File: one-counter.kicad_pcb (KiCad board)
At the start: 2 copper layers, 19.1 x 50.8 mm, 15 parts, among them J1 Conn_01x07-L, J2 Conn_01x07-R, U1 L7805, U2 555-L, U3 555-R, U4 74LS90-L, U5 74LS90-R, U6 7447-L, U7 7447-R, U8 5082-7650-L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

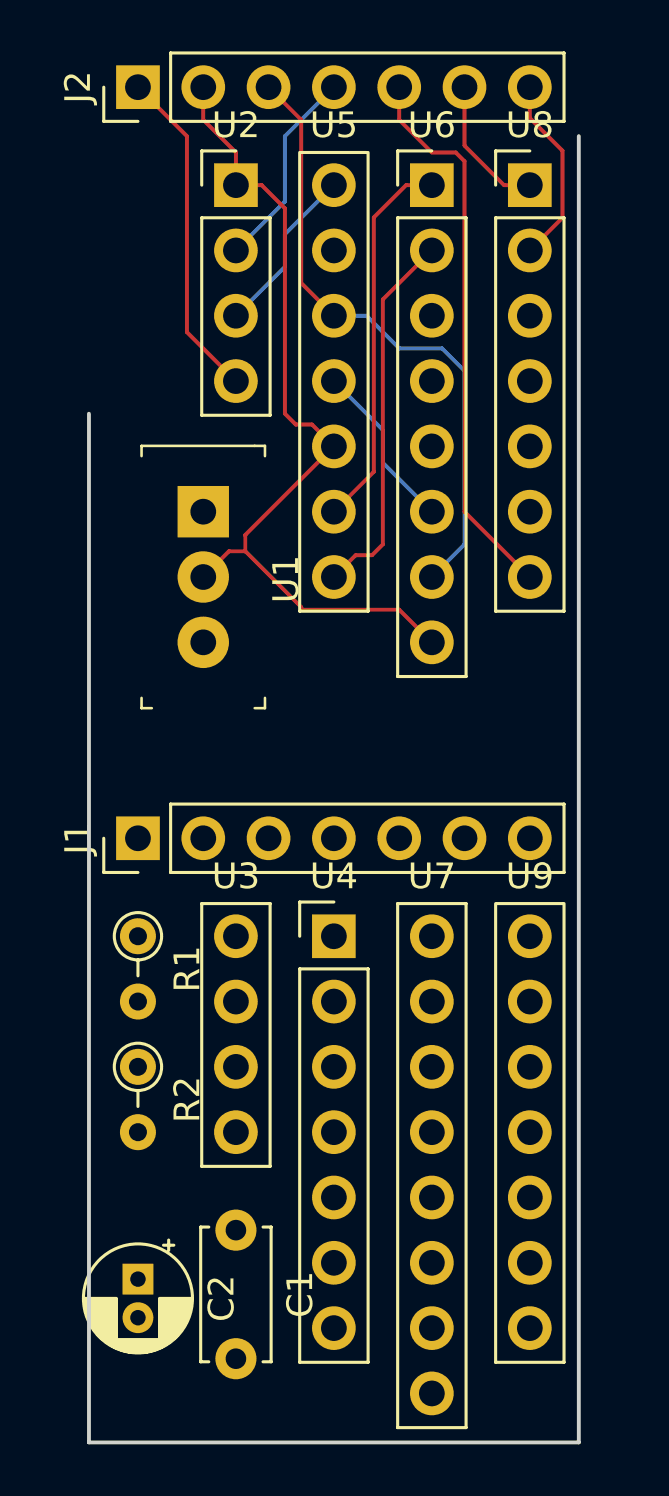
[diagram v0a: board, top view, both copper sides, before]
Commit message: route bottom half
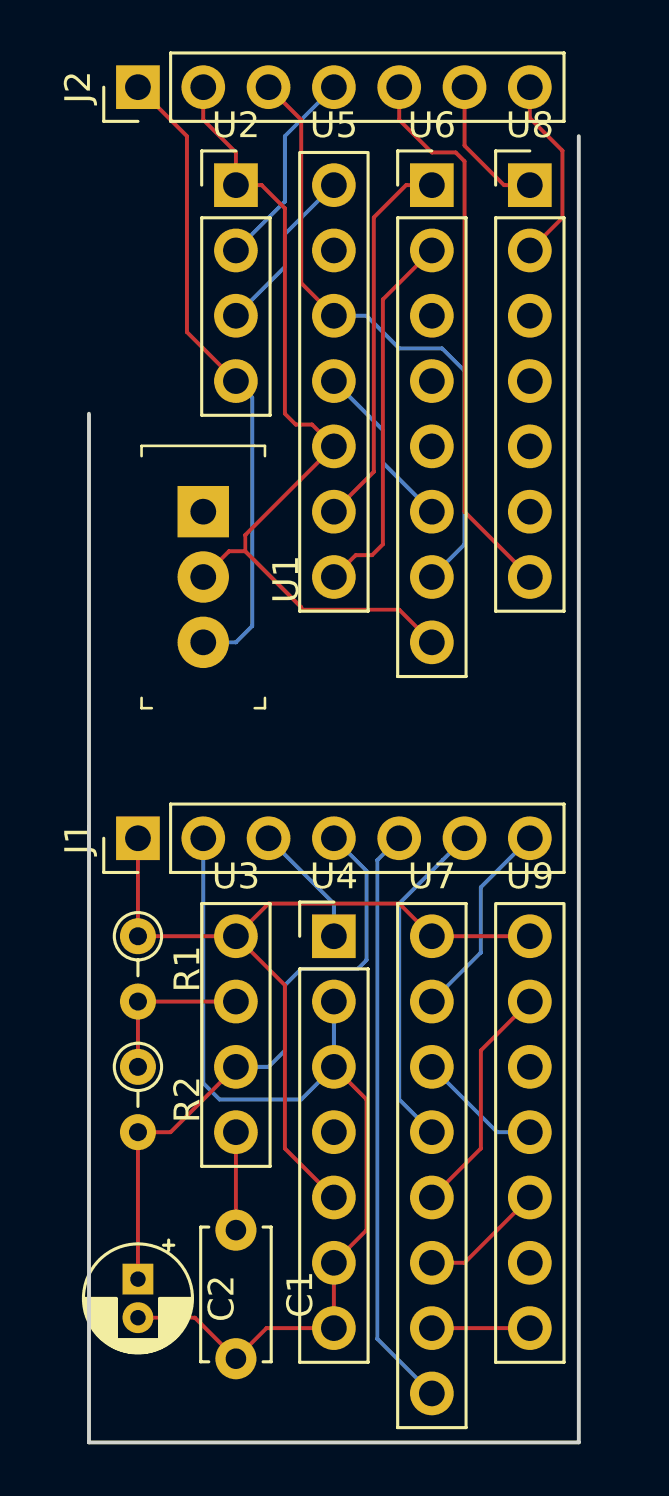
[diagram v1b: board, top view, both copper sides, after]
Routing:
- net +5V: track 13.0 -> 57.4 mm
- net GND: track 33.4 -> 71.3 mm
- net U3-6: track 0.00 -> 24.1 mm
- net U7-9: track 0.00 -> 22.8 mm
- net U7-13: track 0.00 -> 13.0 mm
- net Net-(U7-Pad12): track 0.00 -> 9.20 mm
- net U7-15: track 0.00 -> 7.93 mm
- net Net-(R1-Pad2): track 0.00 -> 6.35 mm
- net U4-1: track 0.00 -> 4.86 mm
- net Net-(U7-Pad14): track 0.00 -> 4.86 mm
- net Net-(U7-Pad11): track 0.00 -> 4.86 mm
- net Net-(U7-Pad10): track 0.00 -> 3.81 mm
- net Net-(C1-Pad1): track 0.00 -> 3.81 mm
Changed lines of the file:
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@@
     (thickness 1.6)
     (drawings 3)
-    (tracks 60)
+    (tracks 121)
     (zones 0)
     (modules 15)
@@
   (gr_line (start 179.705 137.795) (end 160.655 137.795) (layer Edge.Cuts) (width 0.15))
   (gr_line (start 179.705 86.995) (end 179.705 137.795) (layer Edge.Cuts) (width 0.15))
+  (segment (start 166.37 125.73) (end 166.37 129.54) (width 0.1524) (layer F.Cu) (net 1))
   (segment (start 169.330001 98.210001) (end 168.695001 98.210001) (width 0.1524) (layer F.Cu) (net 2))
   (segment (start 170.18 99.06) (end 169.330001 98.210001) (width 0.1524) (layer F.Cu) (net 2))
@@
   (segment (start 168.91 105.315002) (end 166.734999 103.140001) (width 0.1524) (layer F.Cu) (net 2))
   (segment (start 168.91 105.41) (end 168.91 105.315002) (width 0.1524) (layer F.Cu) (net 2))
+  (segment (start 165.1 114.3) (end 165.1 123.825) (width 0.1524) (layer B.Cu) (net 2))
+  (segment (start 165.1 123.825) (end 165.735 124.46) (width 0.1524) (layer B.Cu) (net 2))
+  (segment (start 168.91 124.46) (end 170.18 123.19) (width 0.1524) (layer B.Cu) (net 2))
+  (segment (start 165.735 124.46) (end 168.91 124.46) (width 0.1524) (layer B.Cu) (net 2))
+  (segment (start 170.18 123.19) (end 170.18 120.65) (width 0.1524) (layer B.Cu) (net 2))
+  (segment (start 164.775 132.945) (end 166.37 134.54) (width 0.1524) (layer F.Cu) (net 2))
+  (segment (start 162.56 132.945) (end 164.775 132.945) (width 0.1524) (layer F.Cu) (net 2))
+  (segment (start 167.56 133.35) (end 170.18 133.35) (width 0.1524) (layer F.Cu) (net 2))
+  (segment (start 166.37 134.54) (end 167.56 133.35) (width 0.1524) (layer F.Cu) (net 2))
+  (segment (start 170.18 133.35) (end 170.18 130.81) (width 0.1524) (layer F.Cu) (net 2))
+  (segment (start 171.45 124.46) (end 170.18 123.19) (width 0.1524) (layer F.Cu) (net 2))
+  (segment (start 170.18 130.81) (end 171.45 129.54) (width 0.1524) (layer F.Cu) (net 2))
+  (segment (start 171.45 129.54) (end 171.45 124.46) (width 0.1524) (layer F.Cu) (net 2))
   (segment (start 164.465 86.995) (end 162.56 85.09) (width 0.1524) (layer F.Cu) (net 3))
   (segment (start 166.37 96.52) (end 164.465 94.615) (width 0.1524) (layer F.Cu) (net 3))
   (segment (start 164.465 94.615) (end 164.465 86.995) (width 0.1524) (layer F.Cu) (net 3))
+  (segment (start 165.1 106.68) (end 165.735 106.68) (width 0.25) (layer B.Cu) (net 3))
+  (segment (start 167.005 97.155) (end 166.37 96.52) (width 0.1524) (layer B.Cu) (net 3))
+  (segment (start 167.005 106.045) (end 167.005 97.155) (width 0.1524) (layer B.Cu) (net 3))
+  (segment (start 165.1 106.68) (end 166.37 106.68) (width 0.1524) (layer B.Cu) (net 3))
+  (segment (start 166.37 106.68) (end 167.005 106.045) (width 0.1524) (layer B.Cu) (net 3))
+  (segment (start 162.56 114.3) (end 162.56 118.11) (width 0.1524) (layer F.Cu) (net 3))
+  (segment (start 162.56 118.11) (end 166.37 118.11) (width 0.1524) (layer F.Cu) (net 3))
+  (segment (start 172.72 116.84) (end 173.99 118.11) (width 0.1524) (layer F.Cu) (net 3))
+  (segment (start 166.37 118.11) (end 167.64 116.84) (width 0.1524) (layer F.Cu) (net 3))
+  (segment (start 167.64 116.84) (end 172.72 116.84) (width 0.1524) (layer F.Cu) (net 3))
+  (segment (start 173.99 118.11) (end 177.8 118.11) (width 0.1524) (layer F.Cu) (net 3))
+  (segment (start 168.275 120.015) (end 166.37 118.11) (width 0.1524) (layer F.Cu) (net 3))
+  (segment (start 170.18 128.27) (end 168.275 126.365) (width 0.1524) (layer F.Cu) (net 3))
+  (segment (start 168.275 126.365) (end 168.275 120.015) (width 0.1524) (layer F.Cu) (net 3))
+  (segment (start 166.37 120.65) (end 162.56 120.65) (width 0.1524) (layer F.Cu) (net 4))
+  (segment (start 162.56 120.65) (end 162.56 123.19) (width 0.1524) (layer F.Cu) (net 4))
   (segment (start 168.275 90.805) (end 170.18 88.9) (width 0.1524) (layer B.Cu) (net 5))
   (segment (start 166.37 93.98) (end 168.275 92.075) (width 0.1524) (layer B.Cu) (net 5))
@@
   (segment (start 172.085 99.695) (end 173.99 101.6) (width 0.1524) (layer B.Cu) (net 8))
   (segment (start 172.085 98.425) (end 172.085 99.695) (width 0.1524) (layer B.Cu) (net 8))
+  (segment (start 177.8 133.35) (end 173.99 133.35) (width 0.1524) (layer F.Cu) (net 9))
+  (segment (start 175.26 130.81) (end 177.8 128.27) (width 0.1524) (layer F.Cu) (net 10))
+  (segment (start 173.99 130.81) (end 175.26 130.81) (width 0.1524) (layer F.Cu) (net 10))
+  (segment (start 175.895 122.555) (end 177.8 120.65) (width 0.1524) (layer F.Cu) (net 11))
+  (segment (start 173.99 128.27) (end 175.895 126.365) (width 0.1524) (layer F.Cu) (net 11))
+  (segment (start 175.895 126.365) (end 175.895 122.555) (width 0.1524) (layer F.Cu) (net 11))
+  (segment (start 176.53 125.73) (end 177.8 125.73) (width 0.1524) (layer B.Cu) (net 12))
+  (segment (start 173.99 123.19) (end 176.53 125.73) (width 0.1524) (layer B.Cu) (net 12))
+  (segment (start 170.18 116.84) (end 167.64 114.3) (width 0.1524) (layer B.Cu) (net 13))
+  (segment (start 170.18 118.11) (end 170.18 116.84) (width 0.1524) (layer B.Cu) (net 13))
   (segment (start 170.18 93.98) (end 171.45 93.98) (width 0.1524) (layer B.Cu) (net 14))
   (segment (start 171.45 93.98) (end 172.72 95.25) (width 0.1524) (layer B.Cu) (net 14))
@@
   (segment (start 170.18 93.98) (end 168.91 92.71) (width 0.1524) (layer F.Cu) (net 14))
   (segment (start 168.91 92.71) (end 168.91 86.36) (width 0.1524) (layer F.Cu) (net 14))
+  (segment (start 162.56 131.445) (end 162.56 125.73) (width 0.1524) (layer F.Cu) (net 15))
+  (segment (start 162.56 125.73) (end 163.83 125.73) (width 0.1524) (layer F.Cu) (net 15))
+  (segment (start 163.83 125.73) (end 166.37 123.19) (width 0.1524) (layer F.Cu) (net 15))
+  (segment (start 166.37 123.19) (end 167.64 123.19) (width 0.1524) (layer B.Cu) (net 15))
+  (segment (start 167.64 123.19) (end 168.275 122.555) (width 0.1524) (layer B.Cu) (net 15))
+  (segment (start 168.275 122.555) (end 168.275 120.015) (width 0.1524) (layer B.Cu) (net 15))
+  (segment (start 168.275 120.015) (end 168.91 119.38) (width 0.1524) (layer B.Cu) (net 15))
+  (segment (start 171.107162 119.38) (end 171.45 119.037162) (width 0.1524) (layer B.Cu) (net 15))
+  (segment (start 168.91 119.38) (end 171.107162 119.38) (width 0.1524) (layer B.Cu) (net 15))
+  (segment (start 171.45 115.57) (end 170.18 114.3) (width 0.1524) (layer B.Cu) (net 15))
+  (segment (start 171.45 119.037162) (end 171.45 115.57) (width 0.1524) (layer B.Cu) (net 15))
   (segment (start 166.37 91.44) (end 168.275 89.535) (width 0.1524) (layer B.Cu) (net 16))
   (segment (start 168.275 86.995) (end 170.18 85.09) (width 0.1524) (layer B.Cu) (net 16))
   (segment (start 168.275 89.535) (end 168.275 86.995) (width 0.1524) (layer B.Cu) (net 16))
+  (segment (start 171.870001 115.149999) (end 172.72 114.3) (width 0.1524) (layer B.Cu) (net 17))
+  (segment (start 171.870001 133.770001) (end 171.870001 115.149999) (width 0.1524) (layer B.Cu) (net 17))
+  (segment (start 173.99 135.89) (end 171.870001 133.770001) (width 0.1524) (layer B.Cu) (net 17))
+  (segment (start 174.410001 115.149999) (end 175.26 114.3) (width 0.1524) (layer B.Cu) (net 18))
+  (segment (start 172.72 116.84) (end 174.410001 115.149999) (width 0.1524) (layer B.Cu) (net 18))
+  (segment (start 172.72 124.46) (end 172.72 116.84) (width 0.1524) (layer B.Cu) (net 18))
+  (segment (start 173.99 125.73) (end 172.72 124.46) (width 0.1524) (layer B.Cu) (net 18))
+  (segment (start 173.99 120.65) (end 175.895 118.745) (width 0.1524) (layer B.Cu) (net 19))
+  (segment (start 175.895 116.205) (end 177.8 114.3) (width 0.1524) (layer B.Cu) (net 19))
+  (segment (start 175.895 118.745) (end 175.895 116.205) (width 0.1524) (layer B.Cu) (net 19))
   (segment (start 177.8 86.292081) (end 177.8 85.09) (width 0.1524) (layer F.Cu) (net 20))
   (segment (start 179.07 87.562081) (end 177.8 86.292081) (width 0.1524) (layer F.Cu) (net 20))

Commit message: add board outlines
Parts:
- moved J2 27.5 mm to (177.8, 108.0), turned to 270 degrees
- moved U8 21.6 mm to (162.6, 104.1), turned to 180 degrees
- moved U2 17.0 mm to (174.0, 104.1), turned to 180 degrees
- moved U6 17.0 mm to (166.4, 104.1), turned to 180 degrees
- moved U5 15.2 mm to (170.2, 104.1), turned to 180 degrees
- moved U1 13.9 mm to (175.3, 92.1), turned to 90 degrees
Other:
- board size 19.1 x 50.8 mm -> 19.1 x 53.3 mm

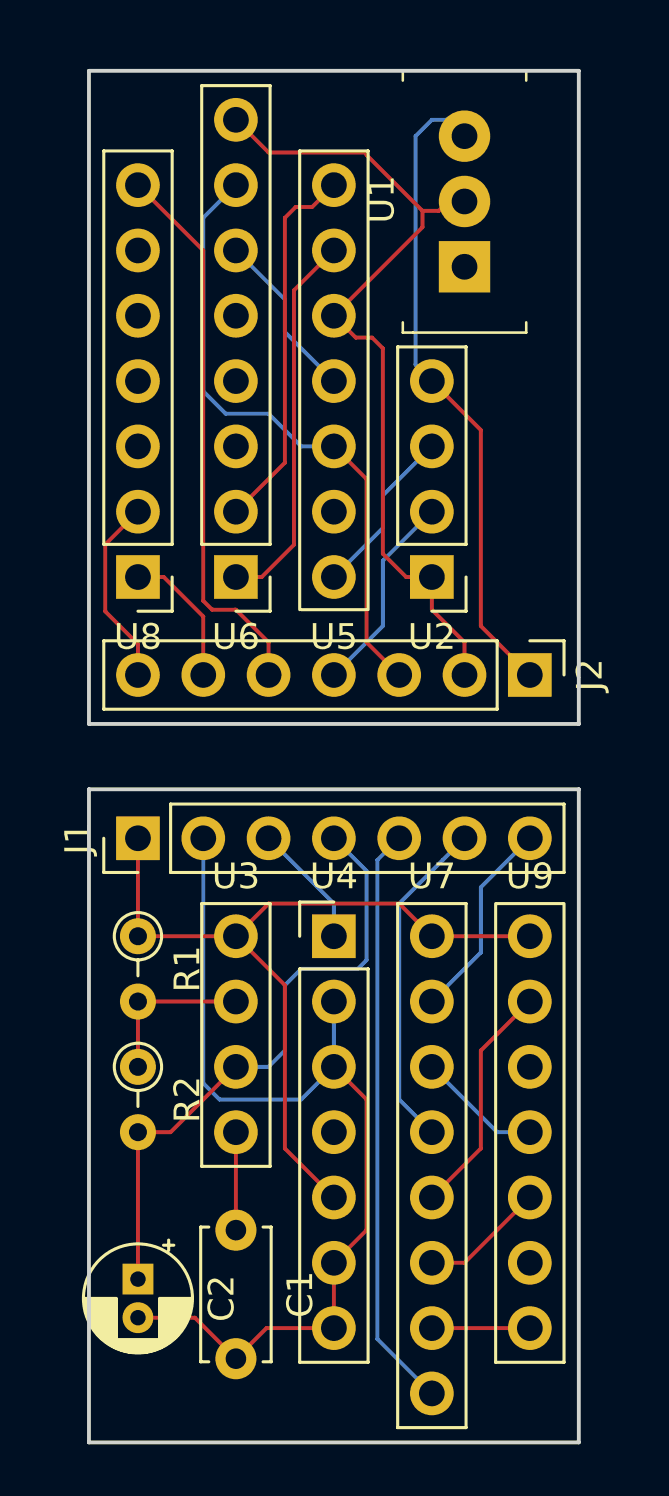
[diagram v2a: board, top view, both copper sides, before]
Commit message: Add design rules, increase track width to 10 mils, change tracks' layers
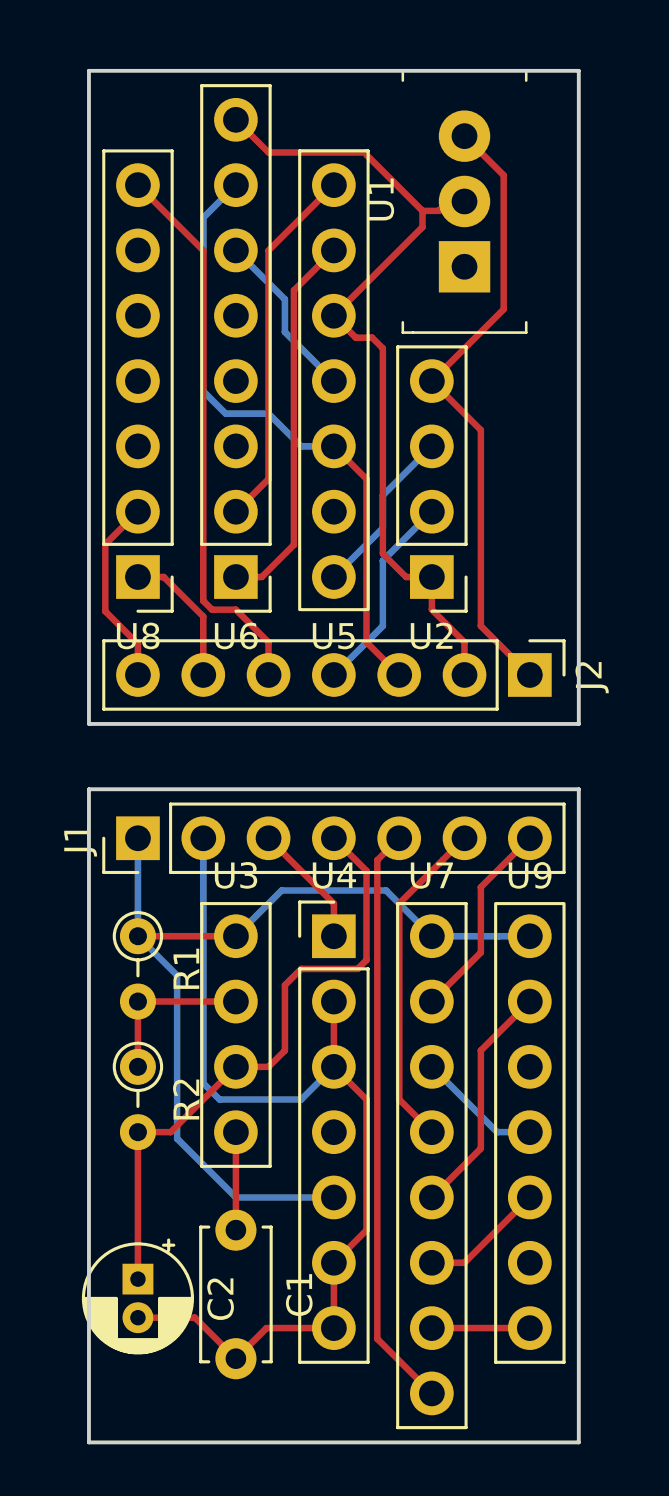
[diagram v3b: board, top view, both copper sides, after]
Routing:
- net +5V: track 57.4 -> 60.4 mm
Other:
- net class Default: clearance 0.2 -> 0.1524; trace_width 0.25 -> 0.1524; via_dia 0.8 -> 0.508; via_drill 0.4 -> 0.254
- net class Large added: clearance 0.254, trace_width 0.254, via_dia 0.508, via_drill 0.254
- rule pad_to_mask_clearance: 0.2 -> 0.0508
- rule trace_clearance: 0.2 -> 0.1524
- rule via_min_size: 0.381 -> 0.508
